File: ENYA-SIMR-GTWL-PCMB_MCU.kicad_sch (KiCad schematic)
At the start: 52 parts, among them J2 TC2050-FP_PROG, J3 PICO_BLADE_1x3_MALE_RA_SMD, J4 PICO_BLADE_1x3_MALE_RA_SMD, J5 PICO_BLADE_1x3_MALE_RA_SMD, J6 PICO_BLADE_1x3_MALE_RA_SMD, Q9 2N7002, U5 STM32F303RET6TR, U6 LM393BIDR, Y2 ABM10_32MHz_10pF_SMD4_2.5x2.0

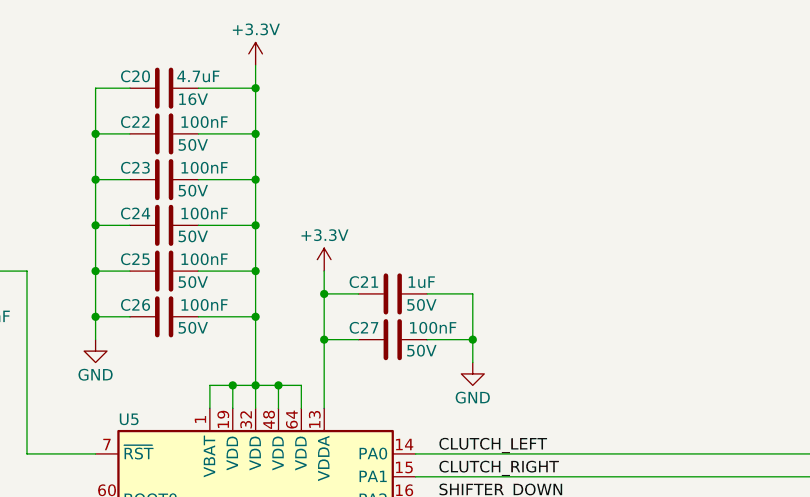
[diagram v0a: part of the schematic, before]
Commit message: using only one diode per selector switch + adding ferrite on VDDA
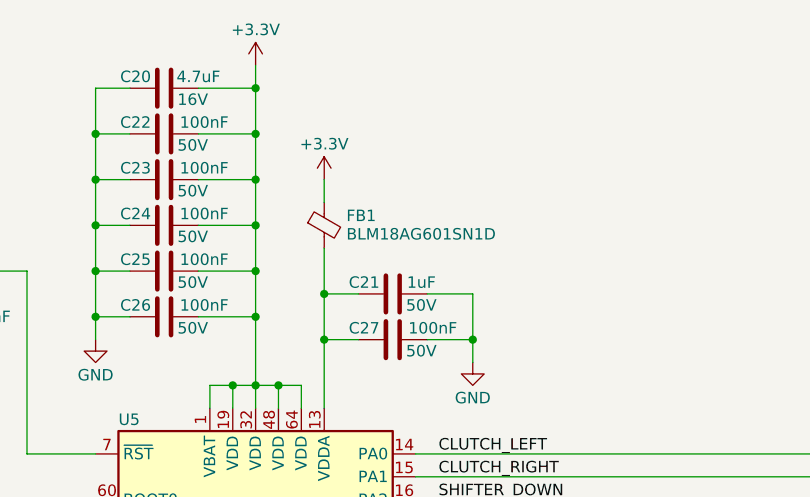
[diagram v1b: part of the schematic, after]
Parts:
- added FB1: 600R_100MHz_0R38_0603, Inductor_SMD:L_0603_1608Metric, symbol ENYA_Ferrite_Smd:600R_100MHz_0R38_0603
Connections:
- net +3.3V: now also FB1.1; no longer C21.1, C27.1, U5.13 (VDDA)
- new net: C21.1, C27.1, FB1.2, U5.13 (VDDA)
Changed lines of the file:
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@@
     (comment 1 "ENYA-SIMR-GTWL-PCMB")
   )
-  (bus_alias "INTERNAL" (members "SWCLK" "SWDIO" "DBG_TX" "DBG_RX" "nRST" "BOOT0" "LEFT_ENC_A" "LEFT_ENC_B" "RIGHT_ENC_A" "RIGHT_ENC_B" "USB1_D+" "USB1_D-" "BTN_ROW0" "BTN_ROW1" "BTN_ROW2" "BTN_ROW3" "BTN_ROW4" "BTN_ROW5" "BTN_ROW6" "BTN_ROW7" "BTN_ROW8" "BTN_ROW9" "BTN_ROW10" "BTN_ROW11" "BTN_COL0" "BTN_COL1" "BTN_COL2" "BTN_COL3" "BTN_COL4" "BTN_COL5" "BTN_COL6" "BTN_COL07" "ALIVE"))
   (bus_alias "ENCODER" (members "LEFT_ENC_A" "LEFT_ENC_B" "RIGHT_ENC_A" "RIGHT_ENC_B"))
+  (bus_alias "INTERNAL" (members "SWCLK" "SWDIO" "DBG_TX" "DBG_RX" "nRST" "BOOT0" "LEFT_ENC_A" "LEFT_ENC_B" "RIGHT_ENC_A" "RIGHT_ENC_B" "USB1_D+" "USB1_D-" "BTN_ROW0" "BTN_ROW1" "BTN_ROW2" "BTN_ROW3" "BTN_ROW4" "BTN_ROW5" "BTN_ROW6" "BTN_ROW7" "BTN_ROW8" "BTN_ROW9" "BTN_ROW10" "BTN_ROW11" "BTN_COL0" "BTN_COL1" "BTN_COL2" "BTN_COL3" "BTN_COL4" "BTN_COL5" "BTN_COL6" "BTN_COL07" "ALIVE"))
   (junction (at 154.94 43.18) (diameter 0) (color 0 0 0 0)
   )
@@
     (stroke (width 0) (type default))
   )
+  (wire (pts (xy 162.56 40.64) (xy 162.56 45.72))
+    (stroke (width 0) (type default))
+  )
   (bus (pts (xy 215.9 170.18) (xy 215.9 172.72))
     (stroke (width 0) (type default))
@@
     (stroke (width 0) (type default))
   )
-  (wire (pts (xy 162.56 43.18) (xy 162.56 45.72))
+  (wire (pts (xy 162.56 33.02) (xy 162.56 35.56))
     (stroke (width 0) (type default))
   )
@@
     )
   )
-  (symbol (lib_id "power:+3.3V") (at 162.56 43.18 0) (unit 1)
+  (symbol (lib_id "power:+3.3V") (at 162.56 33.02 0) (unit 1)
     (in_bom yes) (on_board yes) (dnp no) (fields_autoplaced)
-    (property "Reference" "#PWR028" (at 162.56 46.99 0)
+    (property "Reference" "#PWR028" (at 162.56 36.83 0)
       (effects (font (size 1.27 1.27)) hide)
     )
-    (property "Value" "+3.3V" (at 162.56 39.235 0)
+    (property "Value" "+3.3V" (at 162.56 29.075 0)
       (effects (font (size 1.27 1.27)))
     )
-    (property "Footprint" "" (at 162.56 43.18 0)
+    (property "Footprint" "" (at 162.56 33.02 0)
       (effects (font (size 1.27 1.27)) hide)
     )
-    (property "Datasheet" "" (at 162.56 43.18 0)
+    (property "Datasheet" "" (at 162.56 33.02 0)
       (effects (font (size 1.27 1.27)) hide)
     )
@@
         )
       )
+    )
+  )
+  (symbol (lib_id "ENYA_Ferrite_Smd:600R_100MHz_0R38_0603") (at 162.56 38.1 0) (unit 1)
+    (in_bom yes) (on_board yes) (dnp no) (fields_autoplaced)
+    (property "Reference" "FB1" (at 165.0238 37.0379 0)
+      (effects (font (size 1.27 1.27)) (justify left))
+    )
+    (property "Value" "600R_100MHz_0R38_0603" (at 164.465 39.37 0)
+      (effects (font (size 1.27 1.27)) (justify left) hide)
+    )
+    (property "Footprint" "Inductor_SMD:L_0603_1608Metric" (at 160.782 38.1 90)
+      (effects (font (size 1.27 1.27)) hide)
+    )
+    (property "Datasheet" "~" (at 162.56 38.1 0)
+      (effects (font (size 1.27 1.27)) hide)
+    )
+    (property "Manufacturer" "Murata Electronics" (at 162.56 38.1 0)
+      (effects (font (size 1.27 1.27)) hide)
+    )
+    (property "Manufacturer Part Number" "BLM18AG601SN1D" (at 165.0238 39.0859 0)
+      (effects (font (size 1.27 1.27)) (justify left))
+    )
+    (property "Digi-Key Part Number" "490-1014-1-ND" (at 162.56 38.1 0)
+      (effects (font (size 1.27 1.27)) hide)
+    )
+    (pin "1")
+    (pin "2")
+    (instances
+      (project "ENYA-SIMR-GTWL-PCMB"
+        (path "/6b1a3db9-0352-475b-af94-e6d69f246eea/25e98580-33cf-40e2-b3b5-0167bf965932"
+          (reference "FB1") (unit 1)
+        )
+      )

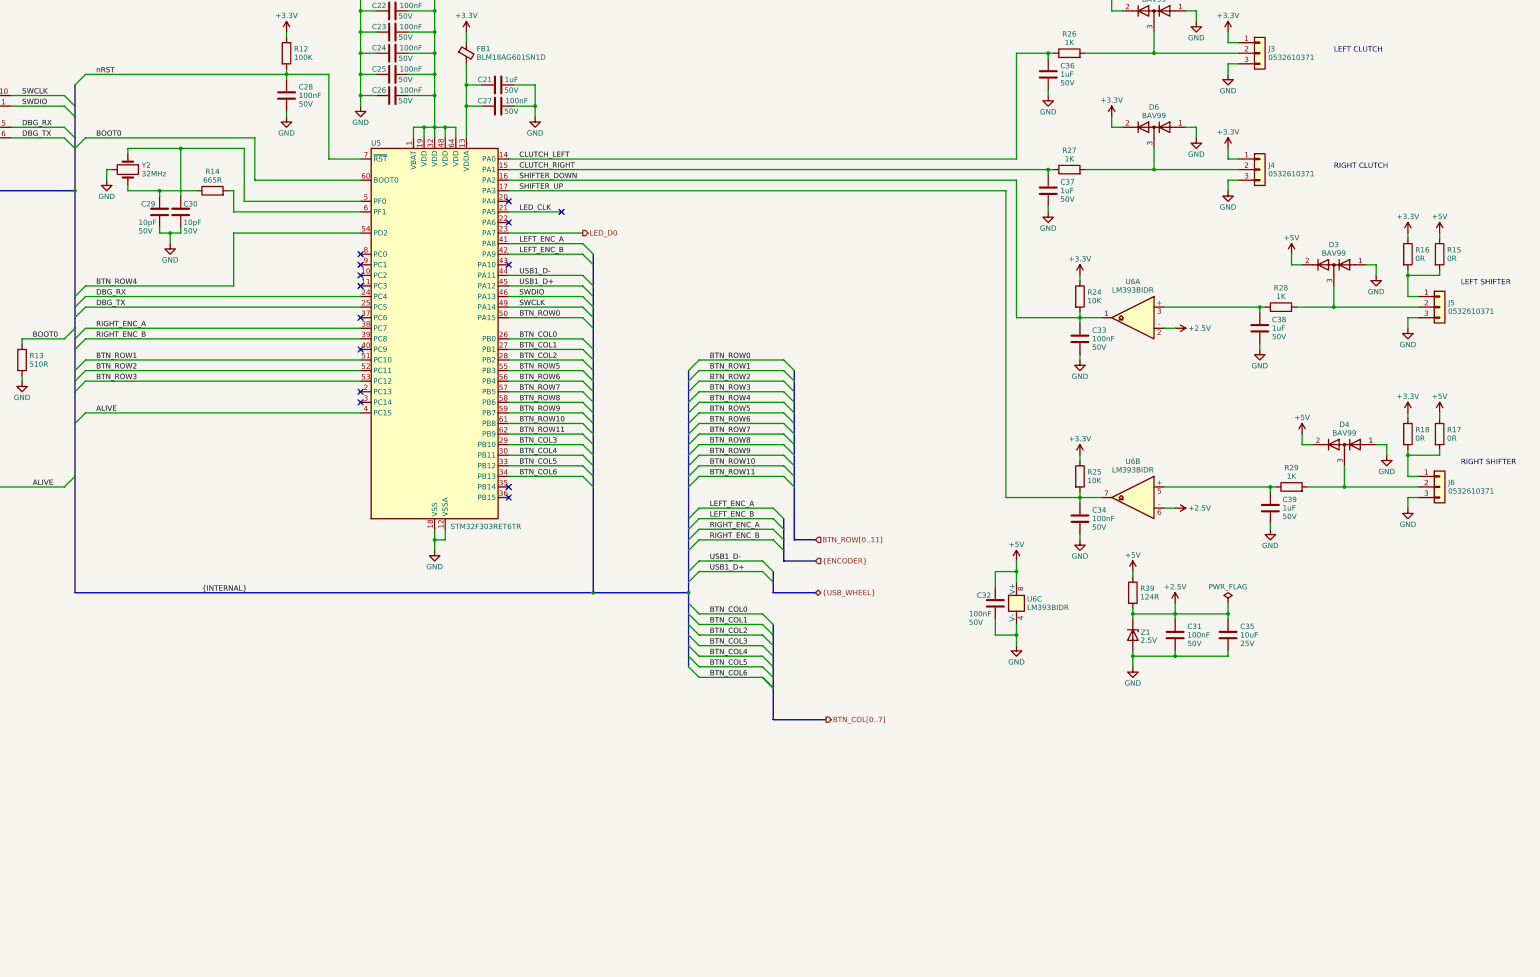
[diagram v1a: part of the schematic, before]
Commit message: rework for encoder instead of selector switch
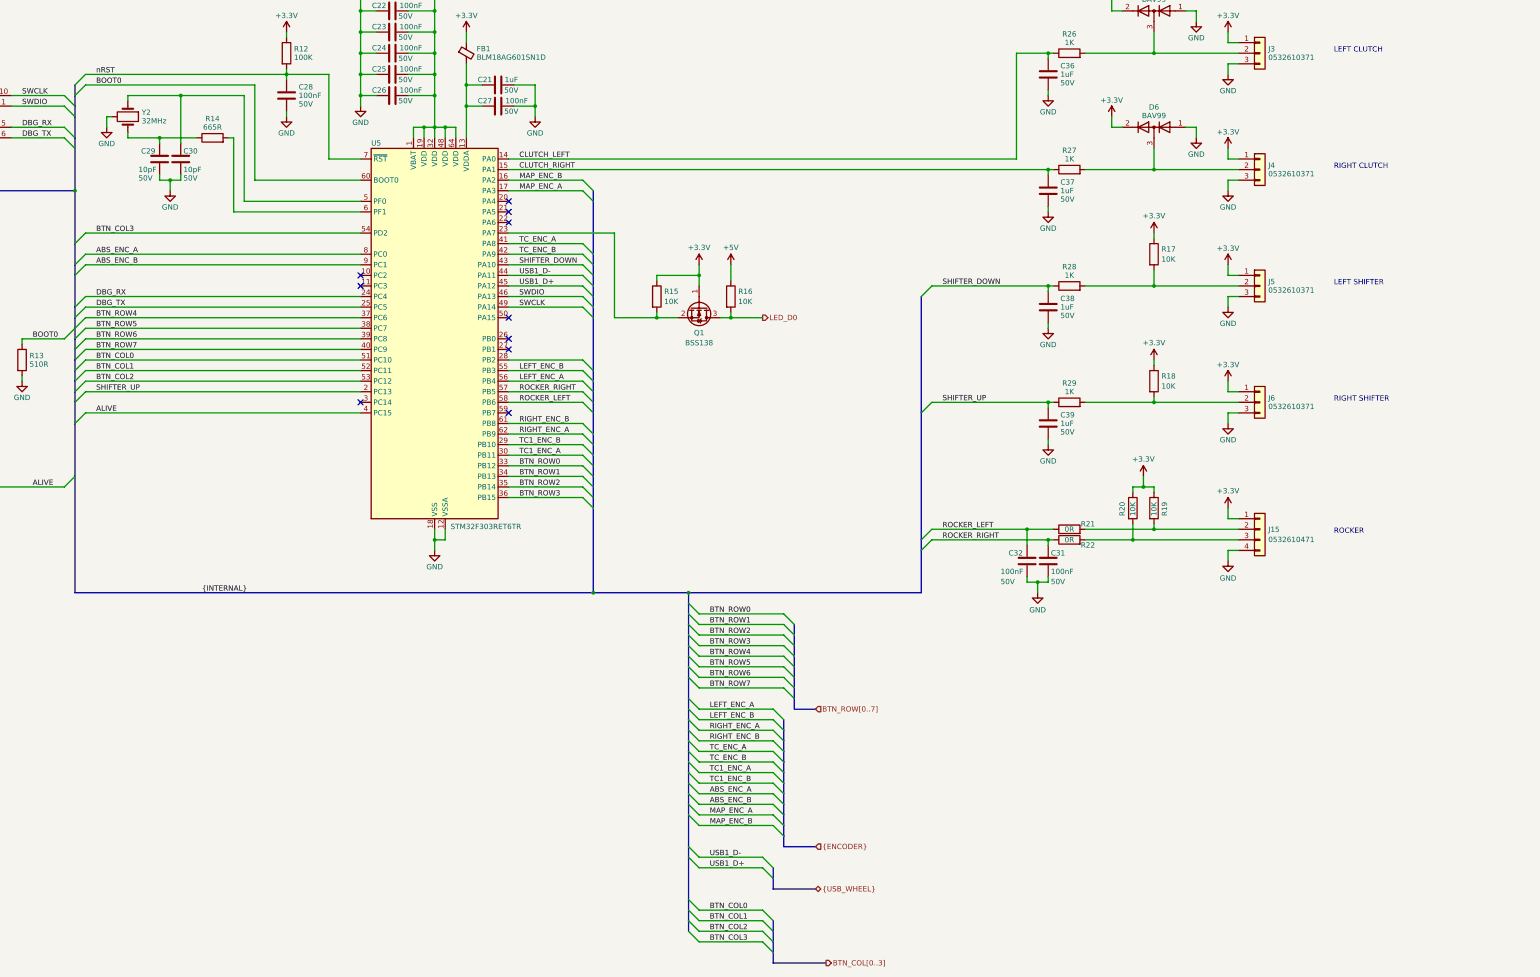
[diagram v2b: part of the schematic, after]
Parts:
- removed C33, C34: 100nF_CER_0603_50V, Capacitor_SMD:C_0603_1608Metric, symbol ENYA_Cap_Smd_50V:100nF_CER_0603_50V
- removed C35: 10uF_CER_1206_25V, Capacitor_SMD:C_1206_3216Metric, symbol ENYA_Cap_Smd_25V:10uF_CER_1206_25V
- removed D3, D4: BAV99_SOT-23, Package_TO_SOT_SMD:SOT-23, symbol ENYA_Diode_Rectifier:BAV99_SOT-23
- removed R15, R16, R17, R18: 0R_0603_100MW, Resistor_SMD:R_0603_1608Metric, symbol ENYA_Res_Smd_100mW:0R_0603_100MW
- removed R24, R25: 10K_0603_100MW, Resistor_SMD:R_0603_1608Metric, symbol ENYA_Res_Smd_100mW:10K_0603_100MW
- removed R39: 124R_0603_100MW, Resistor_SMD:R_0603_1608Metric, symbol ENYA_Res_Smd_100mW:124R_0603_100MW
- removed U6: LM393BIDR, Package_SO:SOIC-8_3.9x4.9mm_P1.27mm, symbol ENYA_Comparator:LM393_SOIC-8
- removed Z1: MMSZ5222BT1G, Diode_SMD:D_SOD-123, symbol ENYA_Diode_Zener:MMSZ5222BT1G_2.5V_500MA_SOD-123
- added J15: PICO_BLADE_1x4_MALE_RA_SMD, ENYA_Connector_PicoBlade:PICO_BLADE_53261_1x4_SMD_RA_1.25MM, symbol ENYA_Connector_PicoBlade:PICO_BLADE_1x4_MALE_RA_SMD
- added Q1: BSS138, Package_TO_SOT_SMD:SOT-23, symbol ENYA_Transistor_N-MOSFET:BSS138
- added R15, R16, R17, R18, R19, R20: 10K_0603_100MW, Resistor_SMD:R_0603_1608Metric, symbol ENYA_Res_Smd_100mW:10K_0603_100MW
- added R21, R22: 0R_0603_100MW, Resistor_SMD:R_0603_1608Metric, symbol ENYA_Res_Smd_100mW:0R_0603_100MW
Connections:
- net BTN_COL5 is gone; now on net BTN_ROW0: U5.33 (PB12)
- net BTN_COL6 is gone; now on net BTN_ROW1: U5.34 (PB13)
- net BTN_ROW10 is gone; now on net RIGHT_ENC_B: U5.61 (PB8)
- net BTN_ROW11 is gone; now on net RIGHT_ENC_A: U5.62 (PB9)
- net +3.3V: now also J5.1 (Pin_1), J6.1 (Pin_1), J15.1 (Pin_1), Q1.1 (G), R15.1, R17.1, R18.1, R19.1, R20.1
- net +5V: now also R16.1; no longer C32.1
- net BTN_COL0: now also U5.51 (PC10); no longer U5.26 (PB0)
- net BTN_COL1: now also U5.52 (PC11); no longer U5.27 (PB1)
- net BTN_COL2: now also U5.53 (PC12); no longer U5.28 (PB2)
- net BTN_COL3: now also U5.54 (PD2); no longer U5.29 (PB10)
- net BTN_ROW0: no longer U5.50 (PA15)
- net BTN_ROW1: no longer U5.51 (PC10)
- net BTN_ROW2: now also U5.35 (PB14); no longer U5.52 (PC11)
- net BTN_ROW3: now also U5.36 (PB15); no longer U5.53 (PC12)
- net BTN_ROW4: now also U5.37 (PC6); no longer U5.54 (PD2)
- net BTN_ROW5: now also U5.38 (PC7); no longer U5.55 (PB3)
- net BTN_ROW6: now also U5.39 (PC8); no longer U5.56 (PB4)
- net BTN_ROW7: now also U5.40 (PC9); no longer U5.57 (PB5)
- net GND: now also J15.4 (Pin_4)
- net LED_D0: now also Q1.3 (D), R16.2; no longer U5.23 (PA7)
- net LEFT_ENC_A: now also U5.56 (PB4); no longer U5.41 (PA8)
- net LEFT_ENC_B: now also U5.55 (PB3); no longer U5.42 (PA9)
- net RIGHT_ENC_A: no longer U5.38 (PC7)
- net RIGHT_ENC_B: no longer U5.39 (PC8)
- net SHIFTER_DOWN: now also C38.1, R28.1, U5.43 (PA10); no longer U5.16 (PA2)
- net SHIFTER_UP: now also C39.1, R29.1, U5.2 (PC13); no longer U5.17 (PA3)
- net at J5.2 (Pin_2), R28.2: now also R17.2
- net at J6.2 (Pin_2), R29.2: now also R18.2
- net ABS_ENC_A: now reaches U5.8 (PC0)
- net ABS_ENC_B: now reaches U5.9 (PC1)
- net +2.5V renamed ROCKER_RIGHT
- net ROCKER_RIGHT: now also U5.57 (PB5), R22.1
- net BTN_COL4 renamed TC1_ENC_A
- net BTN_ROW8 renamed ROCKER_LEFT
- net ROCKER_LEFT: now also C32.1, R21.1
- net BTN_ROW9: no longer names the net of U5.59 (PB7)
- net LED_CLK: no longer names the net of U5.21 (PA5)
- new net: J15.3 (Pin_3), R20.2, R22.2
- new net: J15.2 (Pin_2), R19.2, R21.2
- new net: Q1.2 (S), R15.2, U5.23 (PA7)
- new net MAP_ENC_A: U5.17 (PA3)
- new net MAP_ENC_B: U5.16 (PA2)
- new net TC1_ENC_B: U5.29 (PB10)
- new net TC_ENC_A: U5.41 (PA8)
- new net TC_ENC_B: U5.42 (PA9)
- no-connect marks 14 -> 10
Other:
- note added: "ROCKER"
- moved on the sheet: C29, C30, C38, C39, J5, J6, R14, R28, R29, Y2
